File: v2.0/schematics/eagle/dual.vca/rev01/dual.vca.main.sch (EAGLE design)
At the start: 34 parts, among them IC1 TL084P, IC2 TL082P, Q1 2N3417, Q2 2N3417, Q3 2N3417

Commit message: Swaped Transitors for BC547C; swaped to 100K trim
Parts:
- removed Q1, Q2, Q3: 2N3417, _common:2N3417
- added T1, T2, T3: BC547, transistor:BC547
- R4: value 50K -> 100K
- R7: value 22K -> 5K
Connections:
- net 0V: now also T2.B, T3.C; no longer Q2.B, Q3.C
- net N$13: now also T3.E; no longer Q3.E
- net N$15: now also T3.B; no longer Q3.B
- net N$4: now also T1.B; no longer Q1.B
- net N$5: now also T1.C; no longer Q1.C
- net N$8: now also T2.C; no longer Q2.C
- net N$9: now also T1.E, T2.E; no longer Q1.E, Q2.E
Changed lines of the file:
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@@
 <part name="IC1" library="linear" library_urn="urn:adsk.eagle:library:262" deviceset="TL084" device="P" package3d_urn="urn:adsk.eagle:package:16407/2"/>
 <part name="IC2" library="linear" library_urn="urn:adsk.eagle:library:262" deviceset="TL082" device="P" package3d_urn="urn:adsk.eagle:package:16409/2"/>
-<part name="Q1" library="_common" deviceset="2N3417" device=""/>
-<part name="Q2" library="_common" deviceset="2N3417" device=""/>
-<part name="Q3" library="_common" deviceset="2N3417" device=""/>
 <part name="R1" library="_common" deviceset="R" device="" value="15K"/>
 <part name="R2" library="_common" deviceset="R" device="" value="15K"/>
 <part name="R3" library="rcl" library_urn="urn:adsk.eagle:library:334" deviceset="R-TRIMM" device="3339P" package3d_urn="urn:adsk.eagle:package:23757/1" value="1K"/>
-<part name="R4" library="rcl" library_urn="urn:adsk.eagle:library:334" deviceset="R-TRIMM" device="3339P" package3d_urn="urn:adsk.eagle:package:23757/1" value="50K"/>
+<part name="R4" library="rcl" library_urn="urn:adsk.eagle:library:334" deviceset="R-TRIMM" device="3339P" package3d_urn="urn:adsk.eagle:package:23757/1" value="100K"/>
 <part name="R5" library="rcl" library_urn="urn:adsk.eagle:library:334" deviceset="R-TRIMM" device="3339P" package3d_urn="urn:adsk.eagle:package:23757/1" value="100K"/>
 <part name="P+1" library="supply1" library_urn="urn:adsk.eagle:library:371" deviceset="+12V" device=""/>
@@
 <part name="GND3" library="supply1" library_urn="urn:adsk.eagle:library:371" deviceset="0V" device=""/>
 <part name="GND4" library="supply1" library_urn="urn:adsk.eagle:library:371" deviceset="0V" device=""/>
-<part name="R7" library="_common" deviceset="R" device="" value="22K"/>
+<part name="R7" library="_common" deviceset="R" device="" value="5K"/>
 <part name="R8" library="_common" deviceset="R" device="" value="22K"/>
 <part name="R9" library="_common" deviceset="R" device="" value="100K"/>
@@
 <part name="P-10" library="supply1" library_urn="urn:adsk.eagle:library:371" deviceset="-12V" device=""/>
 <part name="GND8" library="supply1" library_urn="urn:adsk.eagle:library:371" deviceset="0V" device=""/>
+<part name="T1" library="transistor" library_urn="urn:adsk.eagle:library:402" deviceset="BC547" device="" package3d_urn="urn:adsk.eagle:package:28523/2"/>
+<part name="T2" library="transistor" library_urn="urn:adsk.eagle:library:402" deviceset="BC547" device="" package3d_urn="urn:adsk.eagle:package:28523/2"/>
+<part name="T3" library="transistor" library_urn="urn:adsk.eagle:library:402" deviceset="BC547" device="" package3d_urn="urn:adsk.eagle:package:28523/2"/>
 </parts>
 <sheets>
@@
 <attribute name="VALUE" x="53.34" y="30.48" size="1.778" layer="96" rot="MR180"/>
 </instance>
-<instance part="Q1" gate="G$1" x="83.82" y="58.42" smashed="yes">
-<attribute name="NAME" x="89.916" y="55.88" size="1.778" layer="95"/>
-<attribute name="VALUE" x="88.9" y="53.594" size="1.778" layer="96"/>
-</instance>
-<instance part="Q2" gate="G$1" x="114.3" y="58.42" smashed="yes" rot="MR0">
-<attribute name="NAME" x="108.204" y="55.88" size="1.778" layer="95" rot="MR0"/>
-<attribute name="VALUE" x="109.22" y="53.594" size="1.778" layer="96" rot="MR0"/>
-</instance>
-<instance part="Q3" gate="G$1" x="83.82" y="25.4" smashed="yes" rot="MR180">
-<attribute name="NAME" x="89.916" y="27.94" size="1.778" layer="95" rot="MR180"/>
-<attribute name="VALUE" x="88.9" y="30.226" size="1.778" layer="96" rot="MR180"/>
-</instance>
 <instance part="R1" gate="G$1" x="86.36" y="83.82" smashed="yes" rot="R90">
 <attribute name="NAME" x="83.8454" y="83.82" size="1.778" layer="95" rot="R90" align="center"/>
@@
 <instance part="GND8" gate="1" x="134.62" y="45.72" smashed="yes">
 <attribute name="VALUE" x="132.715" y="43.18" size="1.778" layer="96"/>
+</instance>
+<instance part="T1" gate="G$1" x="83.82" y="58.42" smashed="yes">
+<attribute name="NAME" x="88.9" y="58.42" size="1.778" layer="95"/>
+<attribute name="VALUE" x="88.9" y="55.88" size="1.778" layer="96"/>
+</instance>
+<instance part="T2" gate="G$1" x="114.3" y="58.42" smashed="yes" rot="MR0">
+<attribute name="NAME" x="104.14" y="58.42" size="1.778" layer="95" rot="MR0"/>
+<attribute name="VALUE" x="109.22" y="55.88" size="1.778" layer="96" rot="MR0"/>
+</instance>
+<instance part="T3" gate="G$1" x="83.82" y="25.4" smashed="yes" rot="MR180">
+<attribute name="NAME" x="81.28" y="33.02" size="1.778" layer="95" rot="MR180"/>
+<attribute name="VALUE" x="76.2" y="30.48" size="1.778" layer="96" rot="MR180"/>
 </instance>
 </instances>
@@
 </segment>
 <segment>
-<pinref part="Q2" gate="G$1" pin="B"/>
-<wire x1="119.38" y1="58.42" x2="121.92" y2="58.42" width="0.1524" layer="91"/>
 <pinref part="GND4" gate="1" pin="0V"/>
 <wire x1="121.92" y1="58.42" x2="121.92" y2="53.34" width="0.1524" layer="91"/>
-</segment>
-<segment>
-<pinref part="Q3" gate="G$1" pin="C"/>
-<pinref part="GND3" gate="1" pin="0V"/>
-<wire x1="86.36" y1="20.32" x2="86.36" y2="17.78" width="0.1524" layer="91"/>
+<pinref part="T2" gate="G$1" pin="B"/>
+<wire x1="116.84" y1="58.42" x2="121.92" y2="58.42" width="0.1524" layer="91"/>
 </segment>
 <segment>
@@
 <pinref part="GND8" gate="1" pin="0V"/>
 <wire x1="134.62" y1="50.8" x2="134.62" y2="48.26" width="0.1524" layer="91"/>
+</segment>
+<segment>
+<pinref part="T3" gate="G$1" pin="C"/>
+<pinref part="GND3" gate="1" pin="0V"/>
+<wire x1="86.36" y1="20.32" x2="86.36" y2="17.78" width="0.1524" layer="91"/>
 </segment>
 </net>
@@
 <segment>
 <pinref part="R17" gate="G$1" pin="2"/>
-<pinref part="Q1" gate="G$1" pin="B"/>
 <wire x1="73.66" y1="58.42" x2="76.2" y2="58.42" width="0.1524" layer="91"/>
 <pinref part="R18" gate="G$1" pin="2"/>
-<wire x1="76.2" y1="58.42" x2="78.74" y2="58.42" width="0.1524" layer="91"/>
 <wire x1="76.2" y1="53.34" x2="76.2" y2="58.42" width="0.1524" layer="91"/>
+<pinref part="T1" gate="G$1" pin="B"/>
+<wire x1="76.2" y1="58.42" x2="81.28" y2="58.42" width="0.1524" layer="91"/>
 <junction x="76.2" y="58.42"/>
 </segment>
@@
 <net name="N$5" class="0">
 <segment>
-<pinref part="Q1" gate="G$1" pin="C"/>
 <pinref part="R1" gate="G$1" pin="1"/>
-<wire x1="86.36" y1="63.5" x2="86.36" y2="68.58" width="0.1524" layer="91"/>
 <pinref part="R12" gate="G$1" pin="1"/>
 <wire x1="86.36" y1="68.58" x2="86.36" y2="78.74" width="0.1524" layer="91"/>
 <wire x1="86.36" y1="68.58" x2="121.92" y2="68.58" width="0.1524" layer="91"/>
+<pinref part="T1" gate="G$1" pin="C"/>
+<wire x1="86.36" y1="68.58" x2="86.36" y2="63.5" width="0.1524" layer="91"/>
 <junction x="86.36" y="68.58"/>
 </segment>
@@
 <segment>
 <pinref part="R2" gate="G$1" pin="1"/>
-<pinref part="Q2" gate="G$1" pin="C"/>
 <wire x1="111.76" y1="78.74" x2="111.76" y2="76.2" width="0.1524" layer="91"/>
 <pinref part="R11" gate="G$1" pin="1"/>
+<wire x1="111.76" y1="76.2" x2="121.92" y2="76.2" width="0.1524" layer="91"/>
+<pinref part="T2" gate="G$1" pin="C"/>
 <wire x1="111.76" y1="76.2" x2="111.76" y2="63.5" width="0.1524" layer="91"/>
-<wire x1="111.76" y1="76.2" x2="121.92" y2="76.2" width="0.1524" layer="91"/>
 <junction x="111.76" y="76.2"/>
 </segment>
@@
 <net name="N$9" class="0">
 <segment>
-<pinref part="Q2" gate="G$1" pin="E"/>
-<wire x1="111.76" y1="53.34" x2="111.76" y2="50.8" width="0.1524" layer="91"/>
 <wire x1="111.76" y1="50.8" x2="99.06" y2="50.8" width="0.1524" layer="91"/>
-<pinref part="Q1" gate="G$1" pin="E"/>
 <wire x1="99.06" y1="50.8" x2="86.36" y2="50.8" width="0.1524" layer="91"/>
-<wire x1="86.36" y1="50.8" x2="86.36" y2="53.34" width="0.1524" layer="91"/>
 <pinref part="R6" gate="G$1" pin="2"/>
 <wire x1="99.06" y1="50.8" x2="99.06" y2="48.26" width="0.1524" layer="91"/>
 <junction x="99.06" y="50.8"/>
+<pinref part="T1" gate="G$1" pin="E"/>
+<wire x1="86.36" y1="53.34" x2="86.36" y2="50.8" width="0.1524" layer="91"/>
+<pinref part="T2" gate="G$1" pin="E"/>
+<wire x1="111.76" y1="53.34" x2="111.76" y2="50.8" width="0.1524" layer="91"/>
 </segment>
 </net>
@@
 <pinref part="R19" gate="G$1" pin="2"/>
 <wire x1="99.06" y1="38.1" x2="99.06" y2="33.02" width="0.1524" layer="91"/>
-<pinref part="Q3" gate="G$1" pin="E"/>
 <wire x1="99.06" y1="33.02" x2="99.06" y2="27.94" width="0.1524" layer="91"/>
-<wire x1="86.36" y1="30.48" x2="86.36" y2="33.02" width="0.1524" layer="91"/>
 <wire x1="86.36" y1="33.02" x2="99.06" y2="33.02" width="0.1524" layer="91"/>
 <junction x="99.06" y="33.02"/>
+<pinref part="T3" gate="G$1" pin="E"/>
+<wire x1="86.36" y1="33.02" x2="86.36" y2="30.48" width="0.1524" layer="91"/>
 </segment>
 </net>
@@
 <segment>
 <pinref part="R8" gate="G$1" pin="2"/>
-<pinref part="Q3" gate="G$1" pin="B"/>
 <wire x1="73.66" y1="25.4" x2="76.2" y2="25.4" width="0.1524" layer="91"/>
 <pinref part="R7" gate="G$1" pin="2"/>
-<wire x1="76.2" y1="25.4" x2="78.74" y2="25.4" width="0.1524" layer="91"/>
 <wire x1="76.2" y1="25.4" x2="76.2" y2="20.32" width="0.1524" layer="91"/>
+<pinref part="T3" gate="G$1" pin="B"/>
+<wire x1="76.2" y1="25.4" x2="81.28" y2="25.4" width="0.1524" layer="91"/>
 <junction x="76.2" y="25.4"/>
 </segment>

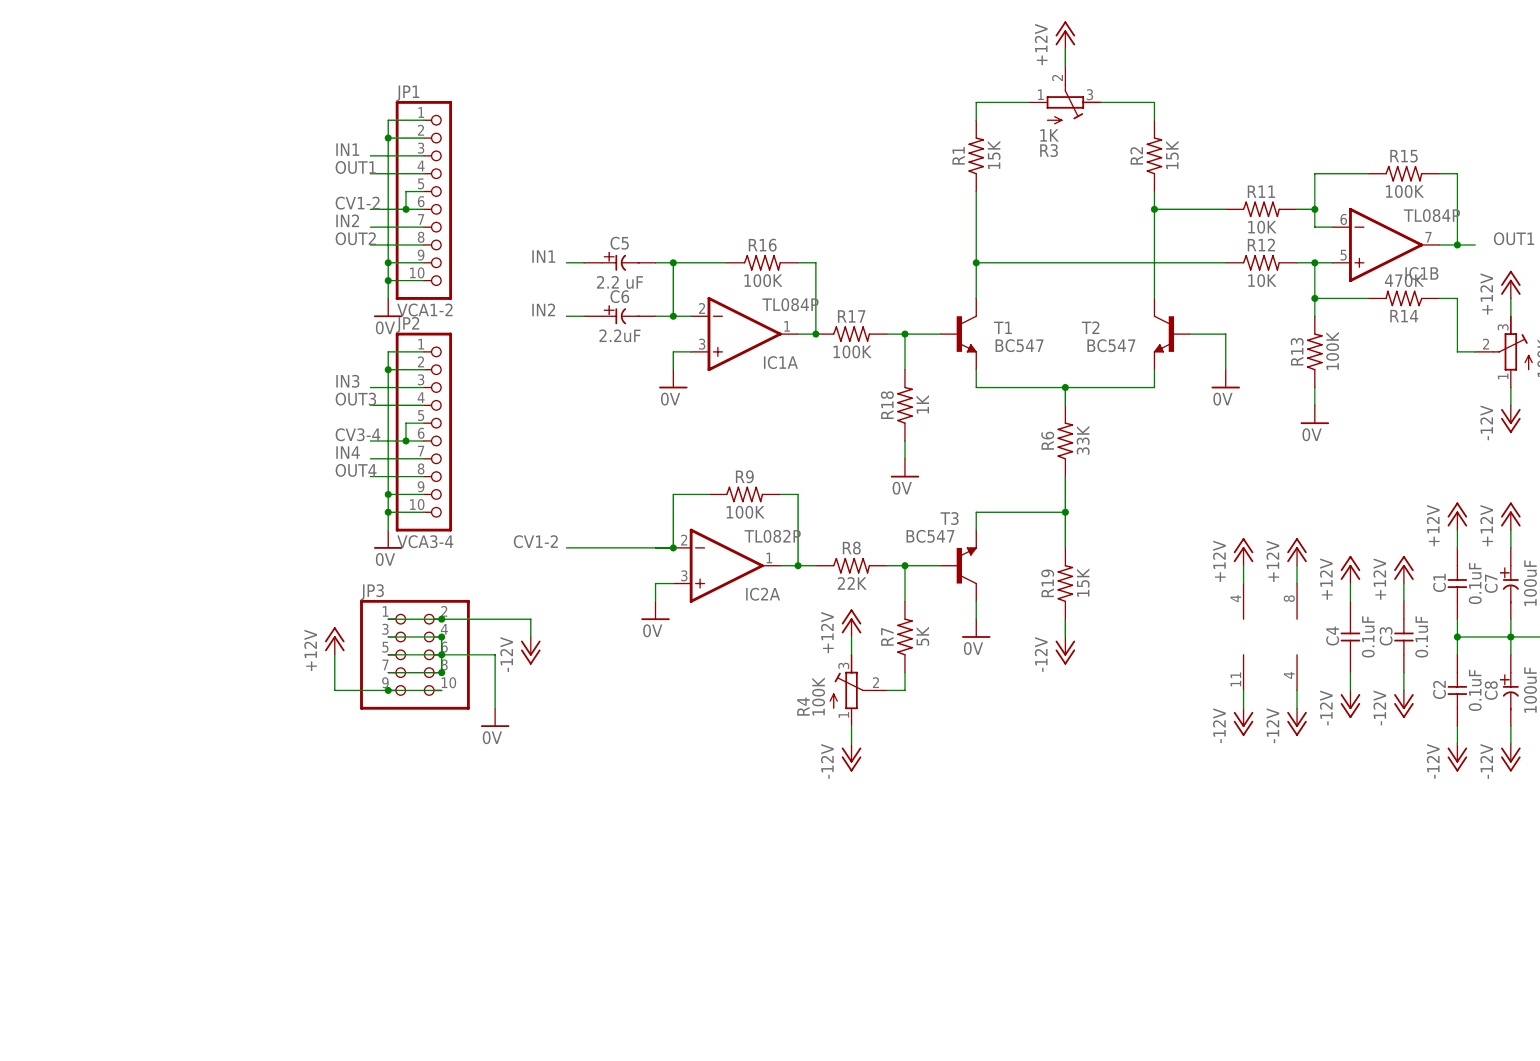
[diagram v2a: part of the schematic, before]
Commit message: Added comparator to dual.vca
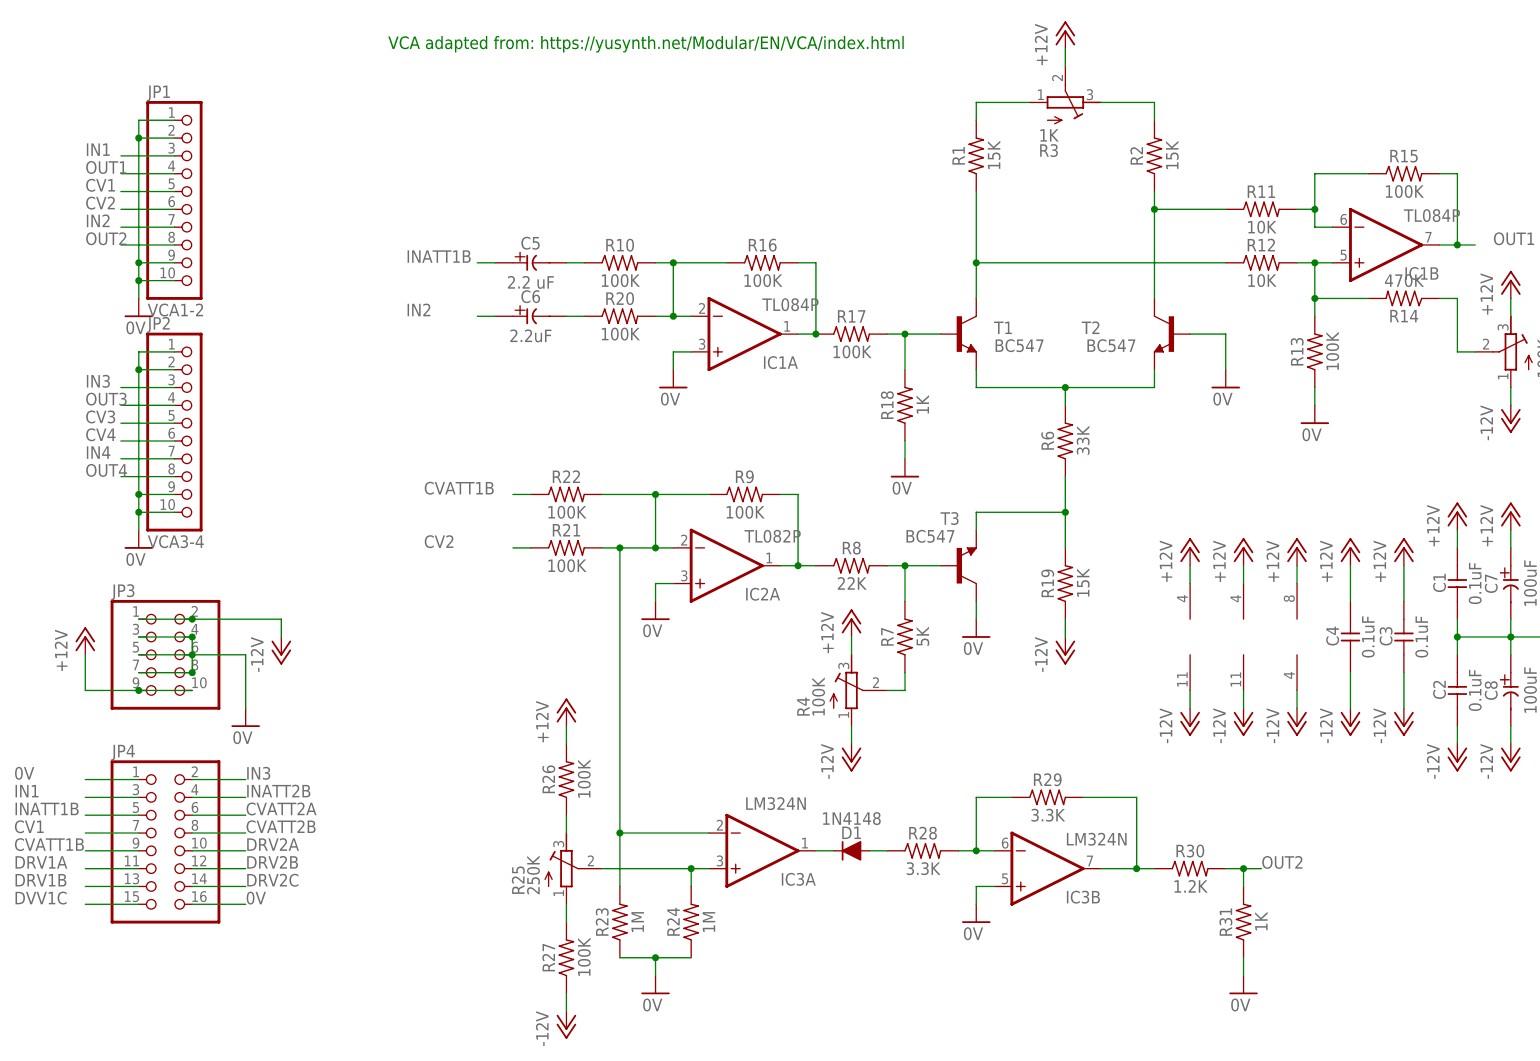
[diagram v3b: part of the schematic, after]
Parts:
- added D1: 1N4148, _common:1N4148
- added IC3: LM324N, linear:LM324N
- added JP4: (no value), pinhead:PINHD-2X8
- added R10, R20, R21, R22, R26, R27: 100K, _common:R
- added R23, R24: 1M, _common:R
- added R25: 250K, rcl:R-TRIMM3339P
- added R28, R29: 3.3K, _common:R
- added R30: 1.2K, _common:R
- added R31: 1K, _common:R
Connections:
- removed net CV1-2: IC2A.-IN, JP1.5, JP1.6, R9.1
- removed net CV3-4: JP2.5, JP2.6
- new net CV1: JP1.5, JP4.7
- new net CV2: JP1.6, R21.1
- new net CV3: JP2.5
- new net CV4: JP2.6
- new net CVATT1B: JP4.9, R22.1
- new net CVATT2A: JP4.6
- new net CVATT2B: JP4.8
- new net DRV1A: JP4.11
- new net DRV1B: JP4.13
- new net DRV2A: JP4.10
- new net DRV2B: JP4.12
- new net DRV2C: JP4.14
- new net DVV1C: JP4.15
- new net INATT1B: C5.+, JP4.5
- new net INATT2B: JP4.4
- new net N$11: C5.-, R10.1
- new net N$14: C6.-, R20.1
- new net N$18: IC3A.+IN, R24.2, R25.S
- new net N$19: IC2A.-IN, IC3A.-IN, R21.2, R22.2, R23.2, R9.1
- new net N$20: R25.E, R26.1
- new net N$21: R25.A, R27.2
- new net N$22: D1.C, IC3A.OUT
- new net N$23: D1.A, R28.1
- new net N$24: IC3B.-IN, R28.2, R29.1
- new net N$25: IC3B.OUT, R29.2, R30.1
- net +12V: now also IC3P.V+, R26.2
- net -12V: now also IC3P.V-, R27.1
- net 0V: now also IC3B.+IN, JP4.1, JP4.16, R23.1, R24.1, R31.1
- net IN1: now also JP4.3; no longer C5.+
- net IN3: now also JP4.2
- net N$1: now also R10.2, R20.2; no longer C5.-, C6.-
- net OUT2: now also R30.2, R31.2
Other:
- note added: "VCA adapted from: https://yusynth.net/Modular/EN/VCA/index.html"
- moved on the sheet: C5, C6, JP1, JP2, JP3
